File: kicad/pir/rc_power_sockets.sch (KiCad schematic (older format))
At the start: 30 parts, among them IC1 ATTINY85, J1 PIR, J2 433MHZ, J3 433MHZ, P1 ICSP, P2 ALT_PWR, Q1 NMOS, Q2 PMOS, U1 MCP1755ST-3302E/DB

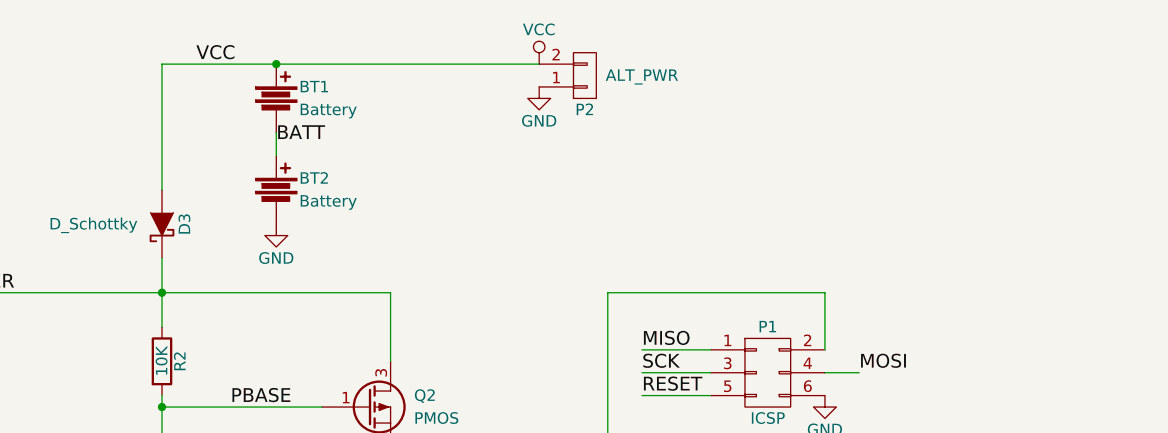
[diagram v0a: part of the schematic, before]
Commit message: Power switch
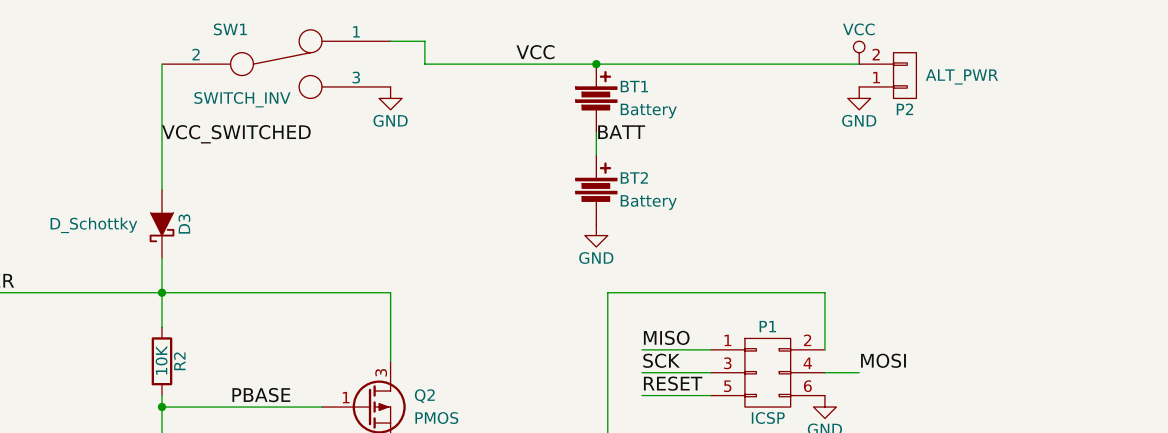
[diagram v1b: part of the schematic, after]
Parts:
- added SW1: SWITCH_INV, Buttons_Switches_ThroughHole:SW_Micro_SPST, symbol SWITCH_INV
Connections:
- net GND: now also SW1.3
- net VCC: now also SW1.1; no longer D3.2 (A)
- new net VCC_SWITCHED: D3.2 (A), SW1.2
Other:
- moved on the sheet: BT1, BT2, P2
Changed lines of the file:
@@
 L Battery BT1
 U 1 1 56F5C9AA
-P 6050 1100
-F 0 "BT1" H 6150 1150 50  0000 L CNN
-F 1 "Battery" H 6150 1050 50  0000 L CNN
-F 2 "theapi_footprints:CR2032H" V 6050 1140 50  0001 C CNN
-F 3 "" V 6050 1140 50  0000 C CNN
-	1    6050 1100
-	1    0    0    -1
-$EndComp
-Wire Wire Line
-	5550 950  7200 950
+P 7450 1100
+F 0 "BT1" H 7550 1150 50  0000 L CNN
+F 1 "Battery" H 7550 1050 50  0000 L CNN
+F 2 "theapi_footprints:CR2032H" V 7450 1140 50  0001 C CNN
+F 3 "" V 7450 1140 50  0000 C CNN
+	1    7450 1100
+	1    0    0    -1
+$EndComp
+Wire Wire Line
+	6700 950  8600 950
 Wire Wire Line
 	5550 950  5550 1500
@@
 L GND #PWR014
 U 1 1 56F5CBEA
-P 6050 1650
-F 0 "#PWR014" H 6050 1400 50  0001 C CNN
-F 1 "GND" H 6050 1500 50  0000 C CNN
-F 2 "" H 6050 1650 50  0000 C CNN
-F 3 "" H 6050 1650 50  0000 C CNN
-	1    6050 1650
+P 7450 1650
+F 0 "#PWR014" H 7450 1400 50  0001 C CNN
+F 1 "GND" H 7450 1500 50  0000 C CNN
+F 2 "" H 7450 1650 50  0000 C CNN
+F 3 "" H 7450 1650 50  0000 C CNN
+	1    7450 1650
 	1    0    0    -1
 $EndComp
@@
 L Battery BT2
 U 1 1 56F65688
-P 6050 1500
-F 0 "BT2" H 6150 1550 50  0000 L CNN
-F 1 "Battery" H 6150 1450 50  0000 L CNN
-F 2 "theapi_footprints:CR2032H" V 6050 1540 50  0001 C CNN
-F 3 "" V 6050 1540 50  0000 C CNN
-	1    6050 1500
-	1    0    0    -1
-$EndComp
-Wire Wire Line
-	6050 1250 6050 1350
-Text Label 6050 1300 0    60   ~ 0
+P 7450 1500
+F 0 "BT2" H 7550 1550 50  0000 L CNN
+F 1 "Battery" H 7550 1450 50  0000 L CNN
+F 2 "theapi_footprints:CR2032H" V 7450 1540 50  0001 C CNN
+F 3 "" V 7450 1540 50  0000 C CNN
+	1    7450 1500
+	1    0    0    -1
+$EndComp
+Wire Wire Line
+	7450 1250 7450 1350
+Text Label 7450 1300 0    60   ~ 0
 BATT
-Text Label 5700 950  0    60   ~ 0
+Text Label 7100 950  0    60   ~ 0
 VCC
 $Comp
@@
 L VCC #PWR016
 U 1 1 56F7F5C9
-P 7200 950
-F 0 "#PWR016" H 7200 800 50  0001 C CNN
-F 1 "VCC" H 7200 1100 50  0000 C CNN
-F 2 "" H 7200 950 50  0000 C CNN
-F 3 "" H 7200 950 50  0000 C CNN
-	1    7200 950
+P 8600 950
+F 0 "#PWR016" H 8600 800 50  0001 C CNN
+F 1 "VCC" H 8600 1100 50  0000 C CNN
+F 2 "" H 8600 950 50  0000 C CNN
+F 3 "" H 8600 950 50  0000 C CNN
+	1    8600 950
 	1    0    0    -1
 $EndComp
@@
 L GND #PWR017
 U 1 1 56F7F83F
-P 7200 1050
-F 0 "#PWR017" H 7200 800 50  0001 C CNN
-F 1 "GND" H 7200 900 50  0000 C CNN
-F 2 "" H 7200 1050 50  0000 C CNN
-F 3 "" H 7200 1050 50  0000 C CNN
-	1    7200 1050
+P 8600 1050
+F 0 "#PWR017" H 8600 800 50  0001 C CNN
+F 1 "GND" H 8600 900 50  0000 C CNN
+F 2 "" H 8600 1050 50  0000 C CNN
+F 3 "" H 8600 1050 50  0000 C CNN
+	1    8600 1050
 	1    0    0    -1
 $EndComp
@@
 L CONN_01X02 P2
 U 1 1 56F7F882
-P 7400 1000
-F 0 "P2" H 7400 1150 50  0000 C CNN
-F 1 "ALT_PWR" H 7650 1000 50  0000 C CNN
-F 2 "Pin_Headers:Pin_Header_Straight_1x02" H 7400 1000 50  0001 C CNN
-F 3 "" H 7400 1000 50  0000 C CNN
-	1    7400 1000
+P 8800 1000
+F 0 "P2" H 8800 1150 50  0000 C CNN
+F 1 "ALT_PWR" H 9050 1000 50  0000 C CNN
+F 2 "Pin_Headers:Pin_Header_Straight_1x02" H 8800 1000 50  0001 C CNN
+F 3 "" H 8800 1000 50  0000 C CNN
+	1    8800 1000
 	1    0    0    1
 $EndComp
-Connection ~ 6050 950
+Connection ~ 7450 950
 $Comp
 L CONN_01X01 MOUNT5
@@
 	1    0    0    -1
 $EndComp
+$Comp
+L SWITCH_INV SW1
+U 1 1 56FBC9B1
+P 6050 950
+F 0 "SW1" H 5850 1100 50  0000 C CNN
+F 1 "SWITCH_INV" H 5900 800 50  0000 C CNN
+F 2 "Buttons_Switches_ThroughHole:SW_Micro_SPST" H 6050 950 50  0001 C CNN
+F 3 "" H 6050 950 50  0000 C CNN
+	1    6050 950
+	1    0    0    -1
+$EndComp
+Wire Wire Line
+	6700 950  6700 850
+Wire Wire Line
+	6700 850  6550 850
+$Comp
+L GND #PWR020
+U 1 1 56FBCCBF
+P 6550 1050
+F 0 "#PWR020" H 6550 800 50  0001 C CNN
+F 1 "GND" H 6550 900 50  0000 C CNN
+F 2 "" H 6550 1050 50  0000 C CNN
+F 3 "" H 6550 1050 50  0000 C CNN
+	1    6550 1050
+	1    0    0    -1
+$EndComp
+Text Label 5550 1300 0    60   ~ 0
+VCC_SWITCHED
 $EndSCHEMATC

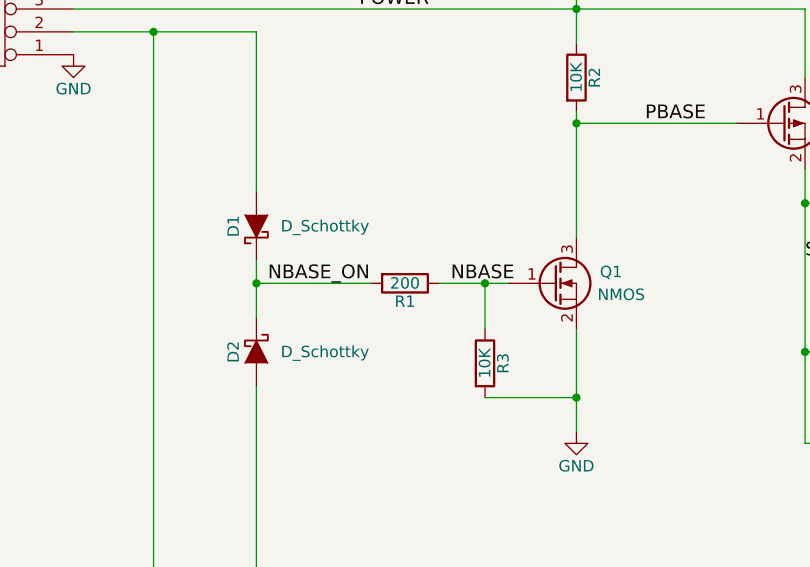
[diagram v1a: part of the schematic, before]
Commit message: Flipped the radio connector to the back
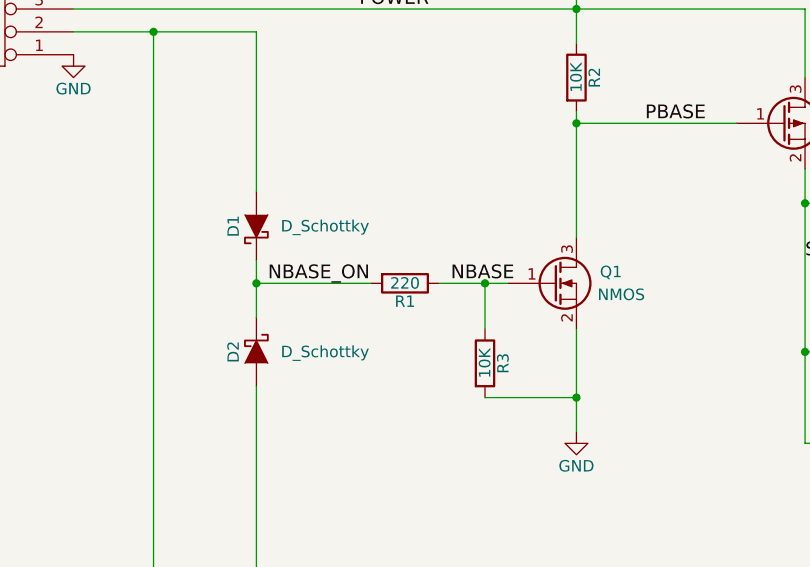
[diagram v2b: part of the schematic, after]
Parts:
- R1: value 200 -> 220
- RV1: footprint Potentiometers:Potentiometer_WirePads_Small -> Pin_Headers:Pin_Header_Straight_1x03
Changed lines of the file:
@@
 P 4800 3150
 F 0 "R1" V 4880 3150 50  0000 C CNN
-F 1 "200" V 4800 3150 50  0000 C CNN
+F 1 "220" V 4800 3150 50  0000 C CNN
 F 2 "Resistors_SMD:R_0805_HandSoldering" V 4730 3150 50  0001 C CNN
 F 3 "" H 4800 3150 50  0000 C CNN
@@
 F 0 "RV1" H 9350 4970 50  0000 C CNN
 F 1 "POT" H 9350 5050 50  0000 C CNN
-F 2 "Potentiometers:Potentiometer_WirePads_Small" H 9350 5050 50  0001 C CNN
+F 2 "Pin_Headers:Pin_Header_Straight_1x03" H 9350 5050 50  0001 C CNN
 F 3 "" H 9350 5050 50  0000 C CNN
 	1    9350 5050

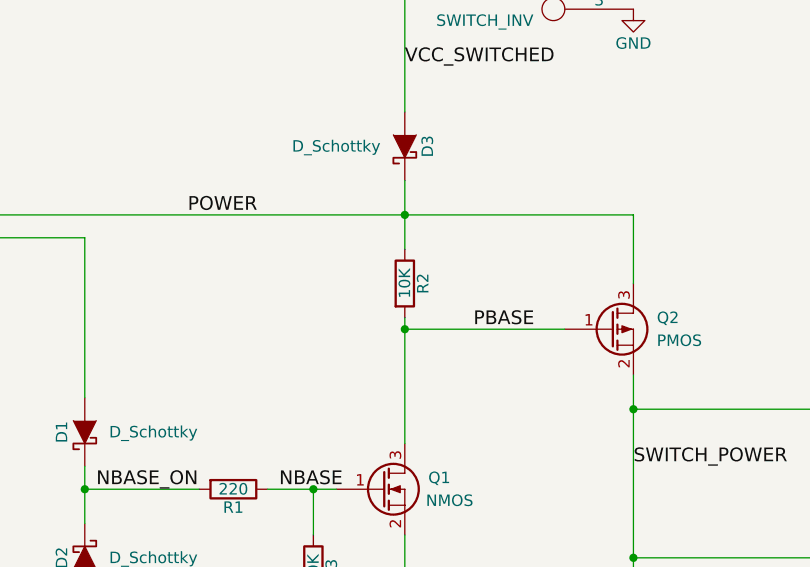
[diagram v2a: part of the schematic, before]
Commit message: 100k pull up on the pmos
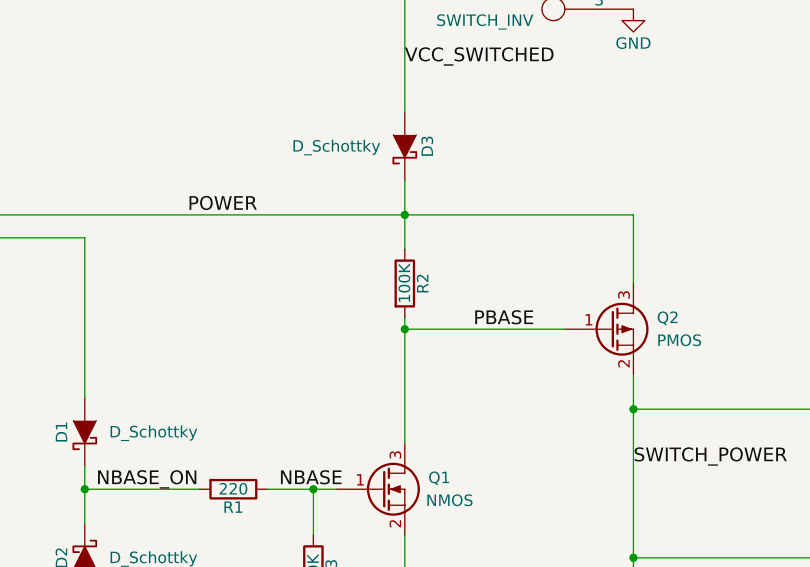
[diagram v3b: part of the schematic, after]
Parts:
- R2: value 10K -> 100K
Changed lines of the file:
@@
 P 5550 2250
 F 0 "R2" V 5630 2250 50  0000 C CNN
-F 1 "10K" V 5550 2250 50  0000 C CNN
+F 1 "100K" V 5550 2250 50  0000 C CNN
 F 2 "Resistors_SMD:R_0805_HandSoldering" V 5480 2250 50  0001 C CNN
 F 3 "" H 5550 2250 50  0000 C CNN

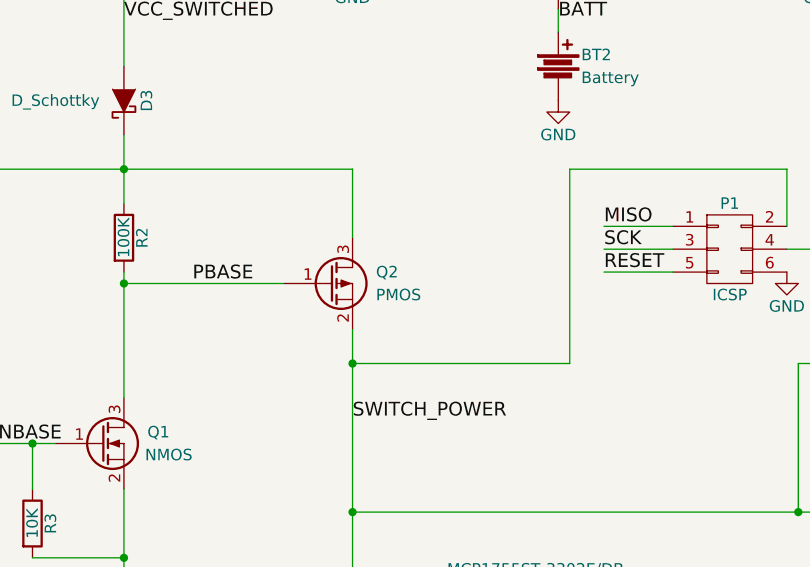
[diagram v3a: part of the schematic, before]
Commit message: Corrected the PMOS
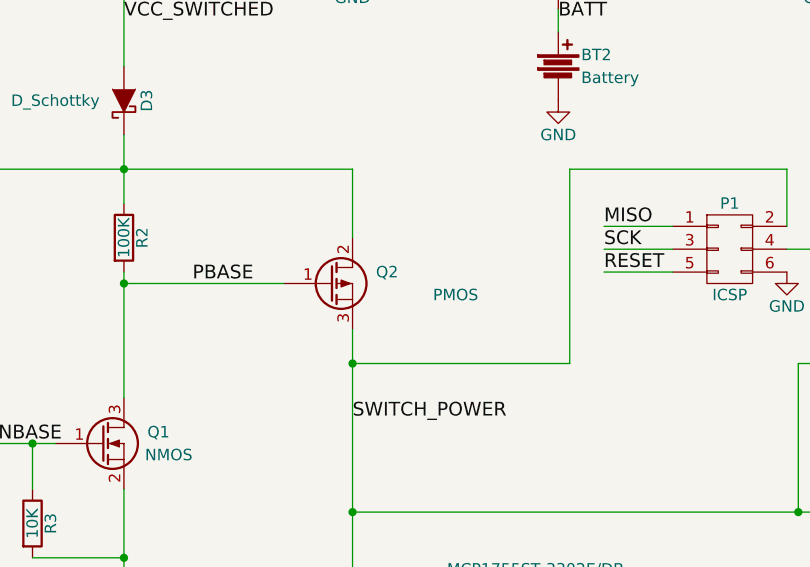
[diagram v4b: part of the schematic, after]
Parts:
- removed Q2: PMOS, TO_SOT_Packages_SMD:SOT-23_Handsoldering, symbol Q_PMOS_GSD
- added Q2: PMOS, symbol Q_PMOS_GDS
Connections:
- net PBASE: now also Q2.1 (G)
- net POWER: now also Q2.2 (D)
- net SWITCH_POWER: now also Q2.3 (S)
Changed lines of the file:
@@
 ADC3
-$Comp
-L Q_PMOS_GSD Q2
-U 1 1 56E815FA
-P 6450 2450
-F 0 "Q2" H 6750 2500 50  0000 R CNN
-F 1 "PMOS" H 6850 2400 50  0000 R CNN
-F 2 "TO_SOT_Packages_SMD:SOT-23_Handsoldering" H 6650 2550 50  0001 C CNN
-F 3 "" H 6450 2450 50  0000 C CNN
-	1    6450 2450
-	1    0    0    -1
-$EndComp
 $Comp
 L Q_NMOS_GSD Q1
@@
 Text Label 5550 1300 0    60   ~ 0
 VCC_SWITCHED
+$Comp
+L Q_PMOS_GDS Q2
+U 1 1 57C74913
+P 6450 2450
+F 0 "Q2" H 6750 2500 50  0000 R CNN
+F 1 "PMOS" H 7100 2400 50  0000 R CNN
+F 2 "" H 6650 2550 50  0000 C CNN
+F 3 "" H 6450 2450 50  0000 C CNN
+	1    6450 2450
+	1    0    0    -1
+$EndComp
 $EndSCHEMATC

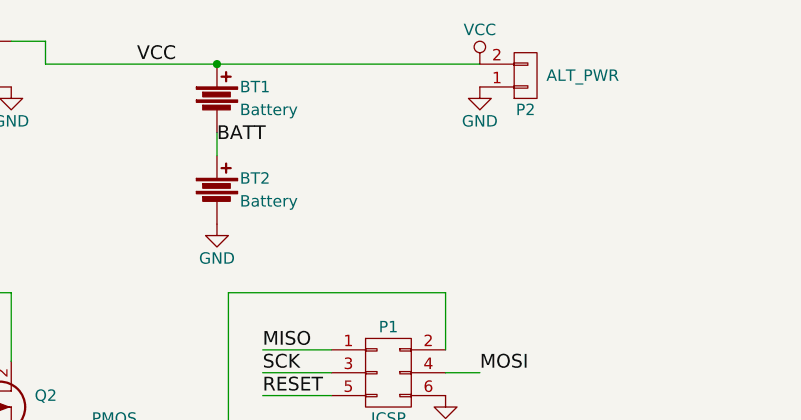
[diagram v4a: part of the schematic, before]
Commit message: Capacitor on the power input
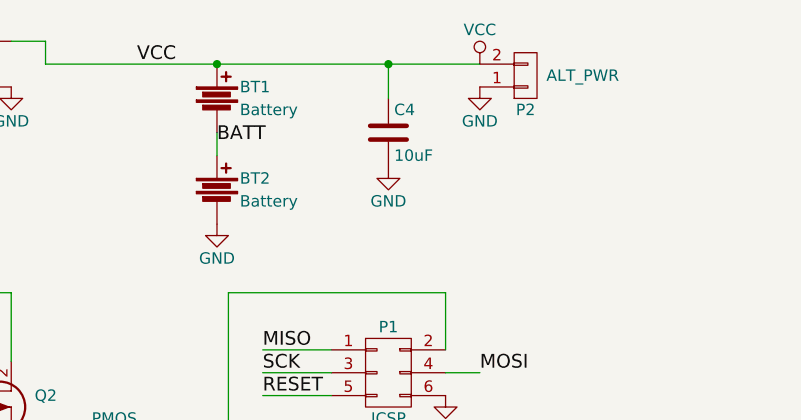
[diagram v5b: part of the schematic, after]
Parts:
- added C4: 10uF, symbol C
- Q2: footprint (none) -> TO_SOT_Packages_SMD:SOT-23_Handsoldering
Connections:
- net GND: now also C4.2
- net VCC: now also C4.1
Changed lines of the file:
@@
 $EndComp
 $Comp
-L GND #PWR01
+L GND #PWR11
 U 1 1 56D4B298
 P 7350 4400
-F 0 "#PWR01" H 7350 4150 50  0001 C CNN
+F 0 "#PWR11" H 7350 4150 50  0001 C CNN
 F 1 "GND" H 7350 4250 50  0000 C CNN
 F 2 "" H 7350 4400 50  0000 C CNN
@@
 $EndComp
 $Comp
-L GND #PWR02
+L GND #PWR9
 U 1 1 56D4D563
 P 5550 3800
-F 0 "#PWR02" H 5550 3550 50  0001 C CNN
+F 0 "#PWR9" H 5550 3550 50  0001 C CNN
 F 1 "GND" H 5550 3650 50  0000 C CNN
 F 2 "" H 5550 3800 50  0000 C CNN
@@
 $EndComp
 $Comp
-L GND #PWR03
+L GND #PWR13
 U 1 1 56D4E393
 P 7600 5550
-F 0 "#PWR03" H 7600 5300 50  0001 C CNN
+F 0 "#PWR13" H 7600 5300 50  0001 C CNN
 F 1 "GND" H 7600 5400 50  0000 C CNN
 F 2 "" H 7600 5550 50  0000 C CNN
@@
 SCK
 $Comp
-L GND #PWR04
+L GND #PWR16
 U 1 1 56D7102B
 P 8450 2400
-F 0 "#PWR04" H 8450 2150 50  0001 C CNN
+F 0 "#PWR16" H 8450 2150 50  0001 C CNN
 F 1 "GND" H 8450 2250 50  0000 C CNN
 F 2 "" H 8450 2400 50  0000 C CNN
@@
 RADIO_DATA
 $Comp
-L GND #PWR05
+L GND #PWR21
 U 1 1 56D83AA4
 P 9400 3550
-F 0 "#PWR05" H 9400 3300 50  0001 C CNN
+F 0 "#PWR21" H 9400 3300 50  0001 C CNN
 F 1 "GND" H 9400 3400 50  0000 C CNN
 F 2 "" H 9400 3550 50  0000 C CNN
@@
 $EndComp
 $Comp
-L GND #PWR06
+L GND #PWR8
 U 1 1 56D83C01
 P 3350 2150
-F 0 "#PWR06" H 3350 1900 50  0001 C CNN
+F 0 "#PWR8" H 3350 1900 50  0001 C CNN
 F 1 "GND" H 3350 2000 50  0000 C CNN
 F 2 "" H 3350 2150 50  0000 C CNN
@@
 $EndComp
 $Comp
-L GND #PWR07
+L GND #PWR15
 U 1 1 56D9DFFD
 P 8250 5500
-F 0 "#PWR07" H 8250 5250 50  0001 C CNN
+F 0 "#PWR15" H 8250 5250 50  0001 C CNN
 F 1 "GND" H 8250 5350 50  0000 C CNN
 F 2 "" H 8250 5500 50  0000 C CNN
@@
 $EndComp
 $Comp
-L GND #PWR08
+L GND #PWR19
 U 1 1 56E80AFC
 P 9350 5200
-F 0 "#PWR08" H 9350 4950 50  0001 C CNN
+F 0 "#PWR19" H 9350 4950 50  0001 C CNN
 F 1 "GND" H 9350 5050 50  0000 C CNN
 F 2 "" H 9350 5200 50  0000 C CNN
@@
 RADIO_DATA
 $Comp
-L GND #PWR09
+L GND #PWR20
 U 1 1 56EEFB0C
 P 9400 2900
-F 0 "#PWR09" H 9400 2650 50  0001 C CNN
+F 0 "#PWR20" H 9400 2650 50  0001 C CNN
 F 1 "GND" H 9400 2750 50  0000 C CNN
 F 2 "" H 9400 2900 50  0000 C CNN
@@
 $EndComp
 $Comp
-L GND #PWR010
+L GND #PWR6
 U 1 1 56F02CD0
 P 1700 1300
-F 0 "#PWR010" H 1700 1050 50  0001 C CNN
+F 0 "#PWR6" H 1700 1050 50  0001 C CNN
 F 1 "GND" H 1700 1150 50  0000 C CNN
 F 2 "" H 1700 1300 50  0000 C CNN
@@
 $EndComp
 $Comp
-L GND #PWR011
+L GND #PWR7
 U 1 1 56F02EF0
 P 2150 1300
-F 0 "#PWR011" H 2150 1050 50  0001 C CNN
+F 0 "#PWR7" H 2150 1050 50  0001 C CNN
 F 1 "GND" H 2150 1150 50  0000 C CNN
 F 2 "" H 2150 1300 50  0000 C CNN
@@
 $EndComp
 $Comp
-L GND #PWR012
+L GND #PWR1
 U 1 1 56F02F76
 P 850 1300
-F 0 "#PWR012" H 850 1050 50  0001 C CNN
+F 0 "#PWR1" H 850 1050 50  0001 C CNN
 F 1 "GND" H 850 1150 50  0000 C CNN
 F 2 "" H 850 1300 50  0000 C CNN
@@
 $EndComp
 $Comp
-L GND #PWR013
+L GND #PWR3
 U 1 1 56F02F82
 P 1300 1300
-F 0 "#PWR013" H 1300 1050 50  0001 C CNN
+F 0 "#PWR3" H 1300 1050 50  0001 C CNN
 F 1 "GND" H 1300 1150 50  0000 C CNN
 F 2 "" H 1300 1300 50  0000 C CNN
@@
 	5550 950  5550 1500
 $Comp
-L GND #PWR014
+L GND #PWR12
 U 1 1 56F5CBEA
 P 7450 1650
-F 0 "#PWR014" H 7450 1400 50  0001 C CNN
+F 0 "#PWR12" H 7450 1400 50  0001 C CNN
 F 1 "GND" H 7450 1500 50  0000 C CNN
 F 2 "" H 7450 1650 50  0000 C CNN
@@
 	2150 5050 1900 5050
 $Comp
-L GND #PWR015
+L GND #PWR4
 U 1 1 56F5DB12
 P 1500 5200
-F 0 "#PWR015" H 1500 4950 50  0001 C CNN
+F 0 "#PWR4" H 1500 4950 50  0001 C CNN
 F 1 "GND" H 1500 5050 50  0000 C CNN
 F 2 "" H 1500 5200 50  0000 C CNN
@@
 Connection ~ 7350 4050
 $Comp
-L VCC #PWR016
+L VCC #PWR17
 U 1 1 56F7F5C9
 P 8600 950
-F 0 "#PWR016" H 8600 800 50  0001 C CNN
+F 0 "#PWR17" H 8600 800 50  0001 C CNN
 F 1 "VCC" H 8600 1100 50  0000 C CNN
 F 2 "" H 8600 950 50  0000 C CNN
@@
 $EndComp
 $Comp
-L GND #PWR017
+L GND #PWR18
 U 1 1 56F7F83F
 P 8600 1050
-F 0 "#PWR017" H 8600 800 50  0001 C CNN
+F 0 "#PWR18" H 8600 800 50  0001 C CNN
 F 1 "GND" H 8600 900 50  0000 C CNN
 F 2 "" H 8600 1050 50  0000 C CNN
@@
 $EndComp
 $Comp
-L GND #PWR018
+L GND #PWR2
 U 1 1 56F8174A
 P 1100 2100
-F 0 "#PWR018" H 1100 1850 50  0001 C CNN
+F 0 "#PWR2" H 1100 1850 50  0001 C CNN
 F 1 "GND" H 1100 1950 50  0000 C CNN
 F 2 "" H 1100 2100 50  0000 C CNN
@@
 $EndComp
 $Comp
-L GND #PWR019
+L GND #PWR5
 U 1 1 56F817AF
 P 1550 2100
-F 0 "#PWR019" H 1550 1850 50  0001 C CNN
+F 0 "#PWR5" H 1550 1850 50  0001 C CNN
 F 1 "GND" H 1550 1950 50  0000 C CNN
 F 2 "" H 1550 2100 50  0000 C CNN
@@
 	6700 850  6550 850
 $Comp
-L GND #PWR020
+L GND #PWR10
 U 1 1 56FBCCBF
 P 6550 1050
-F 0 "#PWR020" H 6550 800 50  0001 C CNN
+F 0 "#PWR10" H 6550 800 50  0001 C CNN
 F 1 "GND" H 6550 900 50  0000 C CNN
 F 2 "" H 6550 1050 50  0000 C CNN
@@
 F 0 "Q2" H 6750 2500 50  0000 R CNN
 F 1 "PMOS" H 7100 2400 50  0000 R CNN
-F 2 "" H 6650 2550 50  0000 C CNN
+F 2 "TO_SOT_Packages_SMD:SOT-23_Handsoldering" H 6650 2550 50  0001 C CNN
 F 3 "" H 6450 2450 50  0000 C CNN
 	1    6450 2450
 	1    0    0    -1
 $EndComp
+$Comp
+L C C4
+U 1 1 57C74F77
+P 8200 1250
+F 0 "C4" H 8225 1350 50  0000 L CNN
+F 1 "10uF" H 8225 1150 50  0000 L CNN
+F 2 "" H 8238 1100 50  0000 C CNN
+F 3 "" H 8200 1250 50  0000 C CNN
+	1    8200 1250
+	1    0    0    -1
+$EndComp
+Wire Wire Line
+	8200 1100 8200 950
+Connection ~ 8200 950
+$Comp
+L GND #PWR14
+U 1 1 57C751C5
+P 8200 1400
+F 0 "#PWR14" H 8200 1150 50  0001 C CNN
+F 1 "GND" H 8200 1250 50  0000 C CNN
+F 2 "" H 8200 1400 50  0000 C CNN
+F 3 "" H 8200 1400 50  0000 C CNN
+	1    8200 1400
+	1    0    0    -1
+$EndComp
